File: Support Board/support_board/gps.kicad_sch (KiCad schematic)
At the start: 24 parts, among them U101 NEO-M8N, U102 SC16IS752, X101 3.072MHZ

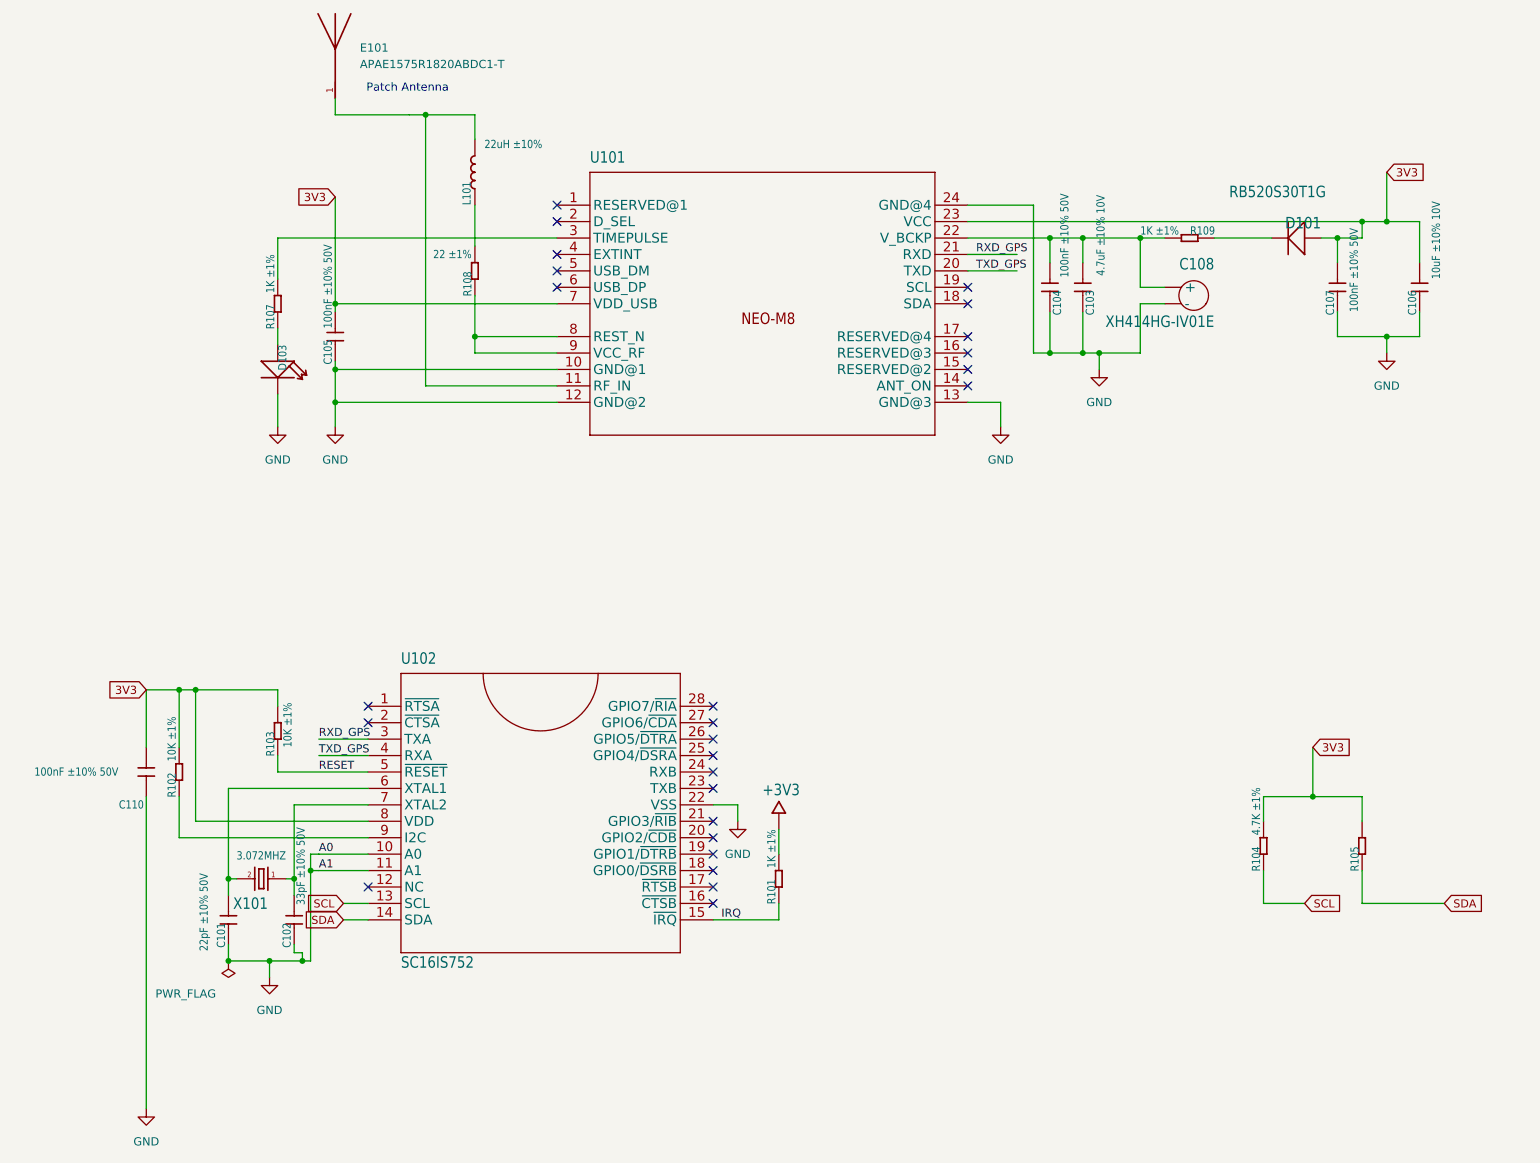
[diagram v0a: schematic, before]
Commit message: Updated PM files and Schematics in the Support Board
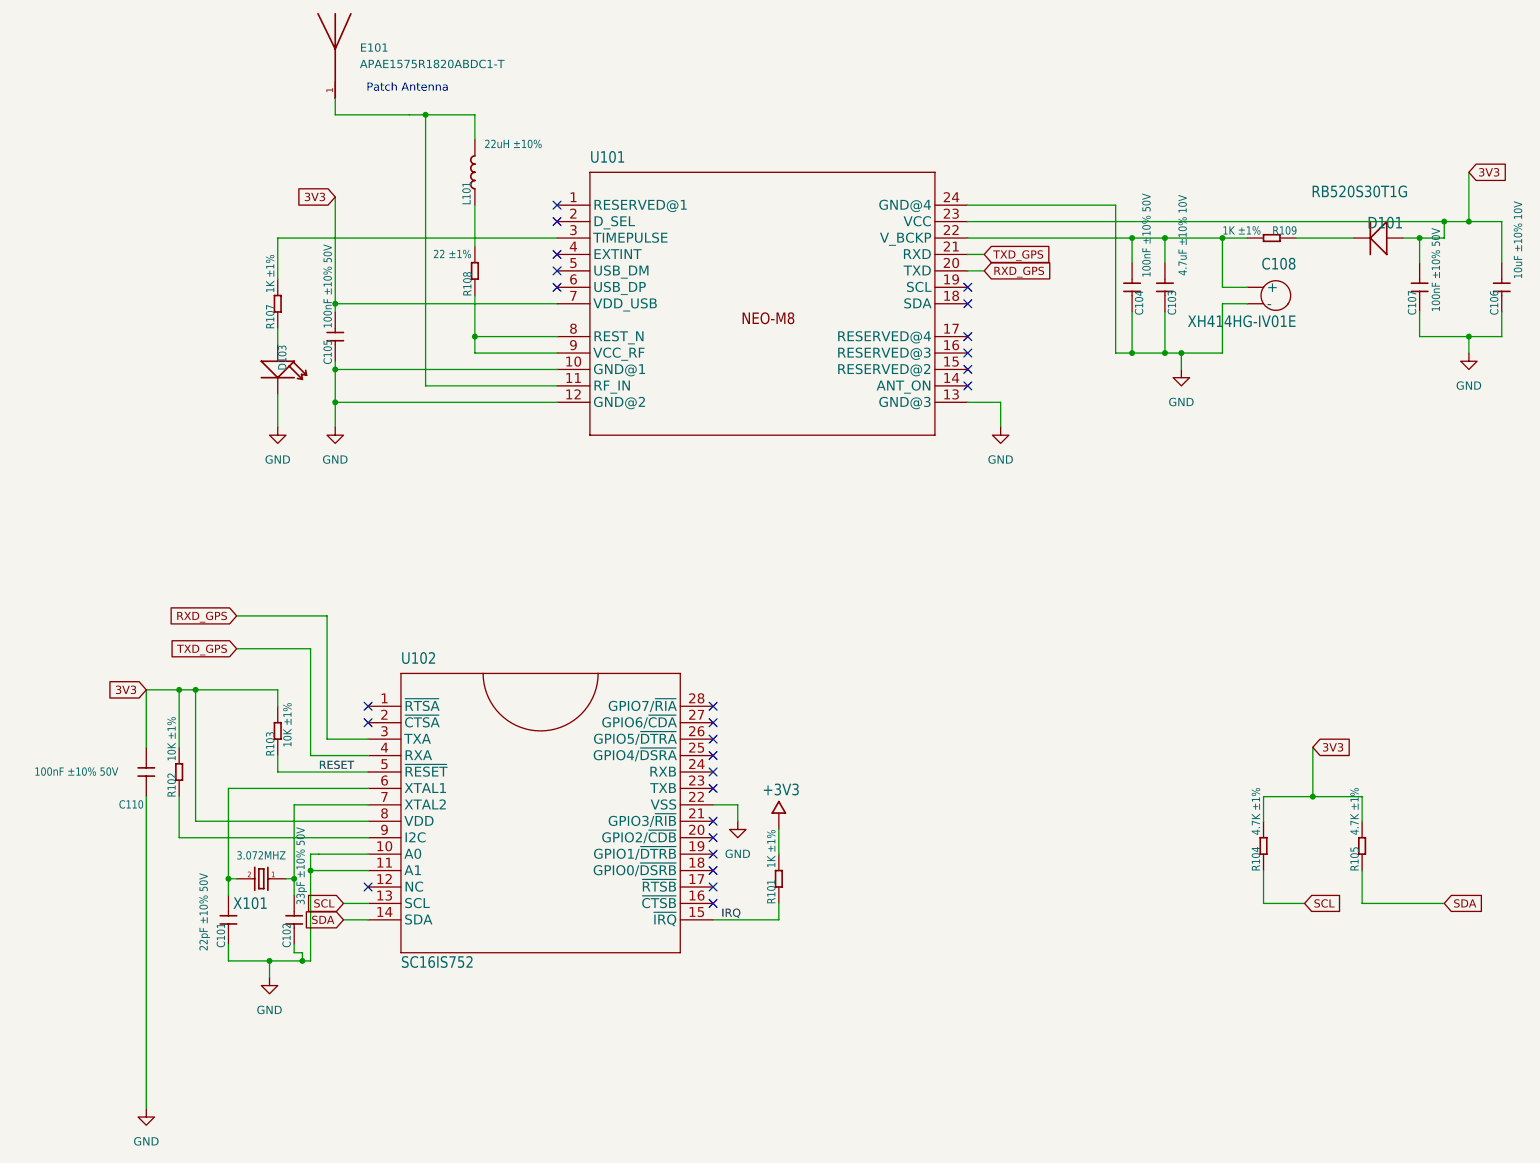
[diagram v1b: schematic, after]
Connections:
- net RXD_GPS: now also U101.20 (TXD); no longer U101.21 (RXD)
- net TXD_GPS: now also U101.21 (RXD); no longer U101.20 (TXD)
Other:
- moved on the sheet: C103, C104, C106, C107, C108, D101, R109
